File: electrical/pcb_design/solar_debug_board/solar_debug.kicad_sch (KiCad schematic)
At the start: 9 parts, among them J1 Molex_430450212, U5 TLV76701DRVx

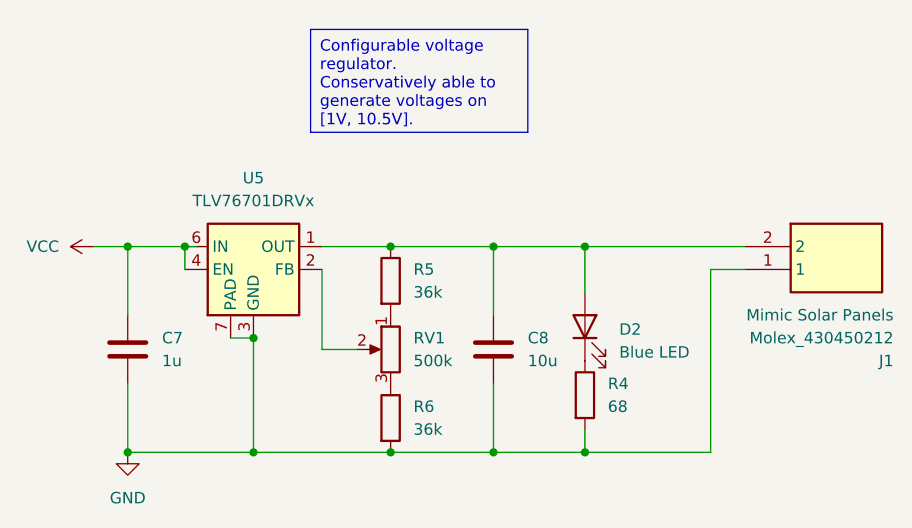
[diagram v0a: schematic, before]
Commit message: Fixed bug in debug header; it was oriented incorrectly. Tweaked schematic layout and part properties. Added production files.
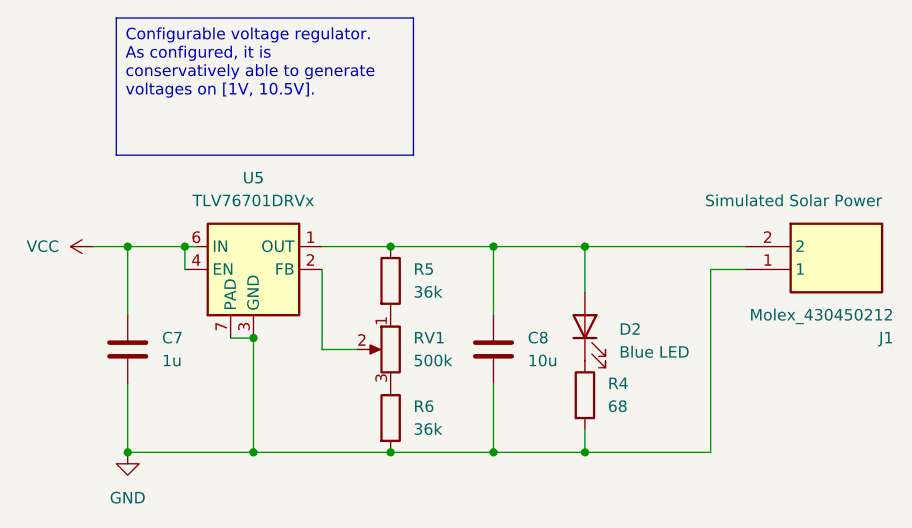
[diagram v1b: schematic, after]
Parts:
- J1: Purpose Mimic Solar Panels -> Simulated Solar Power
- R5, R6, RV1: Active (none) -> Y
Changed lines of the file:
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@@
     (stroke (width 0) (type default))
   )
-  (text_box "Configurable voltage regulator. Conservatively able to generate voltages on [1V, 10.5V]."
-    (at 124.46 49.53 0) (size 24.13 11.43)
+  (text_box "Configurable voltage regulator. As configured, it is conservatively able to generate voltages on [1V, 10.5V]."
+    (at 102.87 48.26 0) (size 33.02 15.24)
     (stroke (width 0) (type default))
     (fill (type none))
@@
     (pin "2")
     (instances
-      (project "debug_core_board"
+      (project "solar_debug_board"
         (path "/476cf7fd-4f82-4468-99c1-e027b17f5088/bbe55d41-cea8-4755-b09e-ba7aff02ad8c"
           (reference "C8") (unit 1)
@@
       (effects (font (size 1.27 1.27)) hide)
     )
-    (pin "2")
-    (pin "1")
-    (instances
-      (project "debug_core_board"
+    (property "Active" "Y" (at 133.35 92.71 0)
+      (effects (font (size 1.27 1.27)) hide)
+    )
+    (pin "2")
+    (pin "1")
+    (instances
+      (project "solar_debug_board"
         (path "/476cf7fd-4f82-4468-99c1-e027b17f5088/bbe55d41-cea8-4755-b09e-ba7aff02ad8c"
           (reference "R6") (unit 1)
@@
     (pin "1")
     (instances
-      (project "debug_core_board"
+      (project "solar_debug_board"
         (path "/476cf7fd-4f82-4468-99c1-e027b17f5088/bbe55d41-cea8-4755-b09e-ba7aff02ad8c"
           (reference "#PWR08") (unit 1)
@@
   (symbol (lib_id "JST B02B-XASK-1 (LF)(SN):B02B-XASK-1__LF__SN_") (at 172.72 73.66 0) (unit 1)
     (in_bom yes) (on_board yes) (dnp no)
-    (property "Reference" "J1" (at 189.23 86.36 0)
-      (effects (font (size 1.27 1.27)) (justify right))
-    )
-    (property "Value" "Molex_430450212" (at 189.23 83.82 0)
+    (property "Reference" "J1" (at 189.23 83.82 0)
+      (effects (font (size 1.27 1.27)) (justify right))
+    )
+    (property "Value" "Molex_430450212" (at 189.23 81.28 0)
       (effects (font (size 1.27 1.27)) (justify right))
     )
@@
       (effects (font (size 1.27 1.27)) (justify left top) hide)
     )
-    (property "Purpose" "Mimic Solar Panels" (at 189.23 81.28 0)
+    (property "Purpose" "Simulated Solar Power" (at 187.96 68.58 0)
       (effects (font (size 1.27 1.27)) (justify right))
     )
@@
     (pin "1")
     (instances
-      (project "debug_core_board"
+      (project "solar_debug_board"
         (path "/476cf7fd-4f82-4468-99c1-e027b17f5088/bbe55d41-cea8-4755-b09e-ba7aff02ad8c"
           (reference "J1") (unit 1)
@@
       (effects (font (size 1.27 1.27)) hide)
     )
+    (property "Active" "Y" (at 133.35 85.09 0)
+      (effects (font (size 1.27 1.27)) hide)
+    )
     (pin "2")
     (pin "3")
     (pin "1")
     (instances
-      (project "debug_core_board"
+      (project "solar_debug_board"
         (path "/476cf7fd-4f82-4468-99c1-e027b17f5088/bbe55d41-cea8-4755-b09e-ba7aff02ad8c"
           (reference "RV1") (unit 1)
@@
       (effects (font (size 1.27 1.27)) hide)
     )
-    (pin "2")
-    (pin "1")
-    (instances
-      (project "debug_core_board"
+    (property "Active" "Y" (at 133.35 77.47 0)
+      (effects (font (size 1.27 1.27)) hide)
+    )
+    (pin "2")
+    (pin "1")
+    (instances
+      (project "solar_debug_board"
         (path "/476cf7fd-4f82-4468-99c1-e027b17f5088/bbe55d41-cea8-4755-b09e-ba7aff02ad8c"
           (reference "R5") (unit 1)
@@
     (pin "1")
     (instances
-      (project "debug_core_board"
+      (project "solar_debug_board"
         (path "/476cf7fd-4f82-4468-99c1-e027b17f5088/bbe55d41-cea8-4755-b09e-ba7aff02ad8c"
           (reference "#PWR021") (unit 1)
@@
     (pin "1")
     (instances
-      (project "debug_core_board"
+      (project "solar_debug_board"
         (path "/476cf7fd-4f82-4468-99c1-e027b17f5088/bbe55d41-cea8-4755-b09e-ba7aff02ad8c"
           (reference "U5") (unit 1)
@@
     (pin "2")
     (instances
-      (project "debug_core_board"
+      (project "solar_debug_board"
         (path "/476cf7fd-4f82-4468-99c1-e027b17f5088/bbe55d41-cea8-4755-b09e-ba7aff02ad8c"
           (reference "D2") (unit 1)
@@
     (pin "2")
     (instances
-      (project "debug_core_board"
+      (project "solar_debug_board"
         (path "/476cf7fd-4f82-4468-99c1-e027b17f5088/bbe55d41-cea8-4755-b09e-ba7aff02ad8c"
           (reference "C7") (unit 1)
@@
     (pin "2")
     (instances
-      (project "debug_core_board"
+      (project "solar_debug_board"
         (path "/476cf7fd-4f82-4468-99c1-e027b17f5088/bbe55d41-cea8-4755-b09e-ba7aff02ad8c"
           (reference "R4") (unit 1)

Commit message: Updated solar debug board DNP list. Part validation continuing.
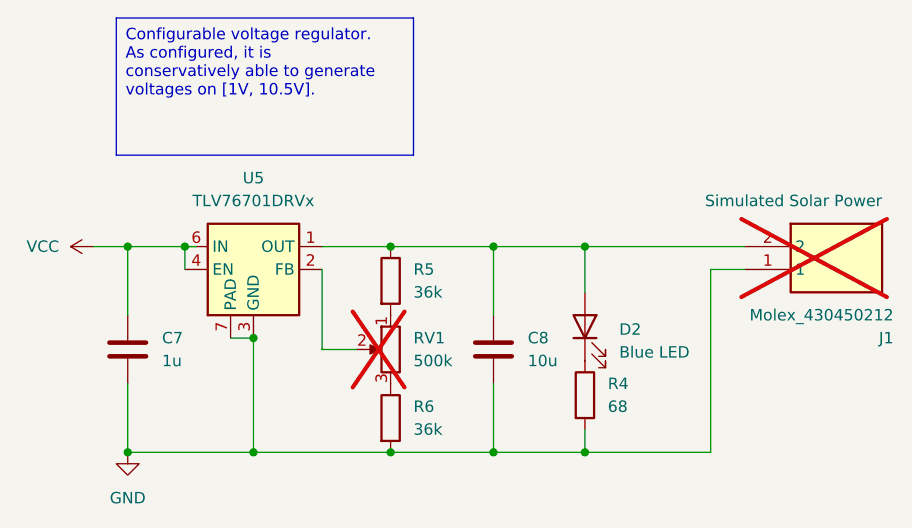
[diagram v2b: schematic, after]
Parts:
- J1: now not fitted
- RV1: footprint Potentiometer_SMD:Potentiometer_Bourns_3314J_Vertical -> Potentiometer_THT:Potentiometer_Bourns_3339H_Vertical; MPN C124628 -> (none); Manufacturer Part Number 3313J-1-504E -> 3339H-1-504LF; now not fitted
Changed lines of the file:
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@@
       (effects (font (size 1.27 1.27)) hide)
     )
-    (property "Datasheet" "https://www.murata.com/en-us/products/productdetail?partno=GRM188R61E106KA73%23" (at 144.78 85.09 0)
+    (property "Datasheet" "~" (at 144.78 85.09 0)
       (effects (font (size 1.27 1.27)) hide)
     )
@@
   )
   (symbol (lib_id "JST B02B-XASK-1 (LF)(SN):B02B-XASK-1__LF__SN_") (at 172.72 73.66 0) (unit 1)
-    (in_bom yes) (on_board yes) (dnp no)
+    (in_bom yes) (on_board yes) (dnp yes)
     (property "Reference" "J1" (at 189.23 83.82 0)
       (effects (font (size 1.27 1.27)) (justify right))
@@
   )
   (symbol (lib_id "Device:R_Potentiometer") (at 133.35 85.09 0) (mirror y) (unit 1)
-    (in_bom yes) (on_board yes) (dnp no)
+    (in_bom yes) (on_board yes) (dnp yes)
     (property "Reference" "RV1" (at 135.89 83.82 0)
       (effects (font (size 1.27 1.27)) (justify right))
@@
       (effects (font (size 1.27 1.27)) (justify right))
     )
-    (property "Footprint" "Potentiometer_SMD:Potentiometer_Bourns_3314J_Vertical" (at 133.35 85.09 0)
+    (property "Footprint" "Potentiometer_THT:Potentiometer_Bourns_3339H_Vertical" (at 133.35 85.09 0)
       (effects (font (size 1.27 1.27)) hide)
     )
@@
       (effects (font (size 1.27 1.27)) hide)
     )
-    (property "MPN" "C124628" (at 133.35 85.09 0)
+    (property "MPN" "" (at 133.35 85.09 0)
       (effects (font (size 1.27 1.27)) hide)
     )
@@
       (effects (font (size 1.27 1.27)) hide)
     )
-    (property "Manufacturer Part Number" "3313J-1-504E" (at 133.35 85.09 0)
+    (property "Manufacturer Part Number" "3339H-1-504LF" (at 133.35 85.09 0)
       (effects (font (size 1.27 1.27)) hide)
     )
@@
       (effects (font (size 1.27 1.27)) hide)
     )
-    (property "Datasheet" "https://octopart.com/datasheet/19-217%2Fbhc-zl1m2ry%2F3t-everlight-56007553" (at 154.94 82.55 0)
-      (effects (font (size 1.27 1.27)) hide)
-    )
+    (property "Datasheet" "~" (at 154.94 82.55 0)
+      (effects (font (size 1.27 1.27)) hide)
+    )

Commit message: Renamed Manfacturer_Name to Manufacturer and Manufacturer_Part_Number to Manufacturer Part Number in order to consolidate the individual fields on parts.
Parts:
- J1: Manufacturer_Name Molex -> (none); Manufacturer_Part_Number 430450212 -> (none)
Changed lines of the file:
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@@
       (effects (font (size 1.27 1.27)) (justify left top) hide)
     )
-    (property "Manufacturer_Name" "Molex" (at 189.23 568.58 0)
+    (property "Manufacturer" "Molex" (at 189.23 568.58 0)
       (effects (font (size 1.27 1.27)) (justify left top) hide)
     )
-    (property "Manufacturer_Part_Number" "430450212" (at 189.23 668.58 0)
+    (property "Manufacturer Part Number" "430450212" (at 189.23 668.58 0)
       (effects (font (size 1.27 1.27)) (justify left top) hide)
     )
